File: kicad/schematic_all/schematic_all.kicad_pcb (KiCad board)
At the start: 2 copper layers, 88.9 x 88.9 mm, 31 parts, among them J1 Power In, SW1 Button 1, SW2 Encoder 1, SW3 Button 2, SW4 Encoder 2, SW5 Button 3, U2 RPi_Pico, U3 RDA5807M_Module, U4 LM386

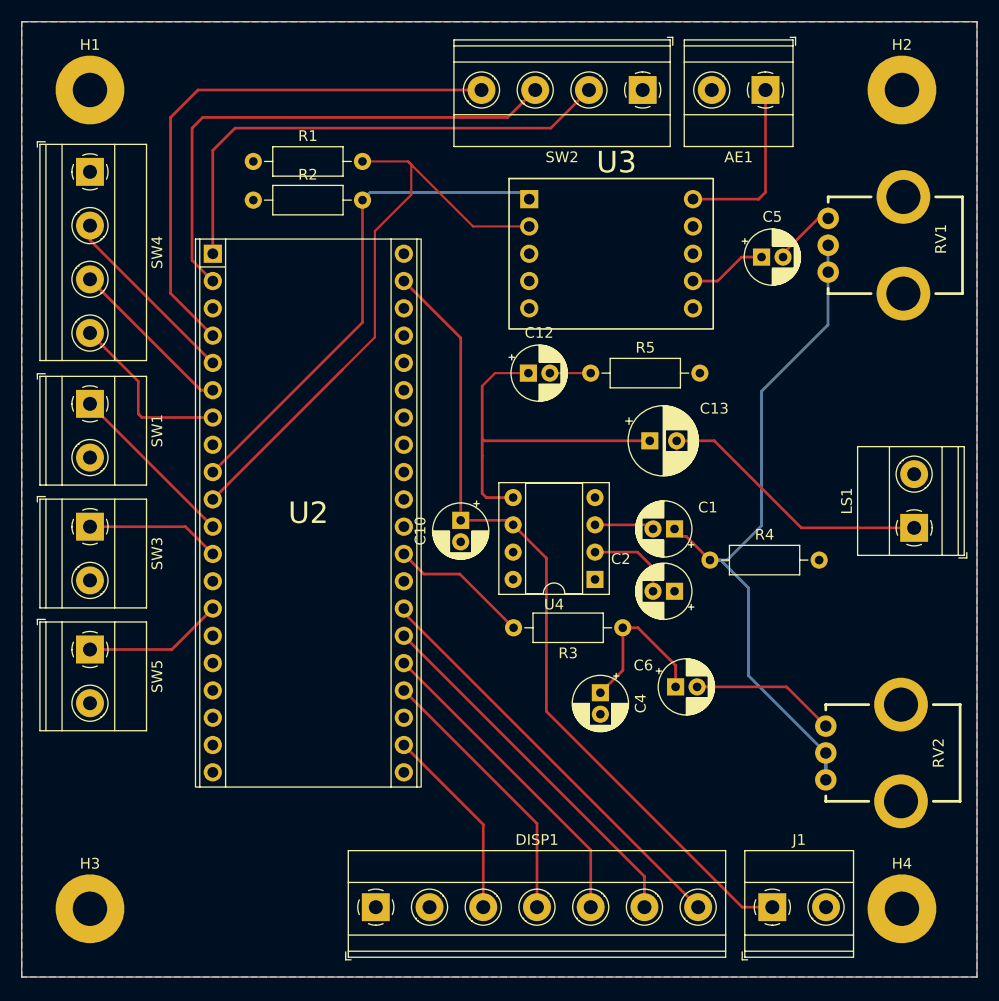
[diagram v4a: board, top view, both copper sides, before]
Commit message: Added 12V supply + linear regulator to step-down to 5V
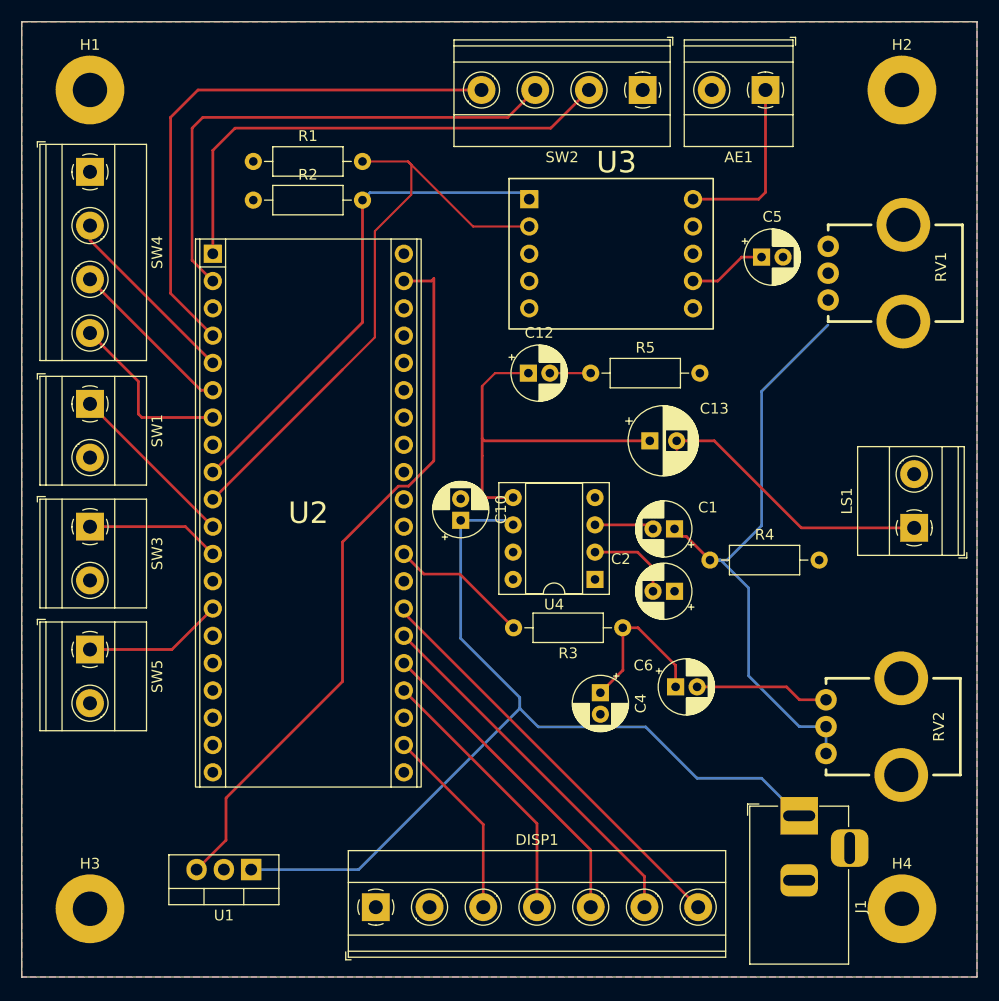
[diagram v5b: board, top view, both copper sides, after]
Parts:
- added U1: L7805, Package_TO_SOT_THT:TO-220-3_Vertical, F.Cu at (78.5, 117.0)
- J1: value Power In -> Barrel_Jack_MountingPin; footprint TerminalBlock_Phoenix:TerminalBlock_Phoenix_MKDS-1,5-2_1x02_P5.00mm_Horizontal -> Connector_BarrelJack:BarrelJack_Horizontal
- moved J1 8.86 mm to (129.5, 112.0), turned to 90 degrees
- moved RV1 2.60 mm to (132.2, 61.5)
- moved RV2 2.45 mm to (132.0, 103.7)
- turned C10 to 90 degrees
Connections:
- C10 pad 1: +5V -> +12V
- J1 pad 1: +5V -> +12V
- U4 pad 6: +5V -> +12V
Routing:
- net +12V: track 0.00 -> 86.8 mm
- net Net-(C1-Pad1): track 68.2 -> 56.4 mm
- net +5V: track 76.8 -> 67.6 mm
- net Net-(C5-Pad2): track 6.23 -> 0.32 mm
- net Net-(C6-Pad2): track 13.5 -> 12.5 mm

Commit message: Replaced jack with a terminal block
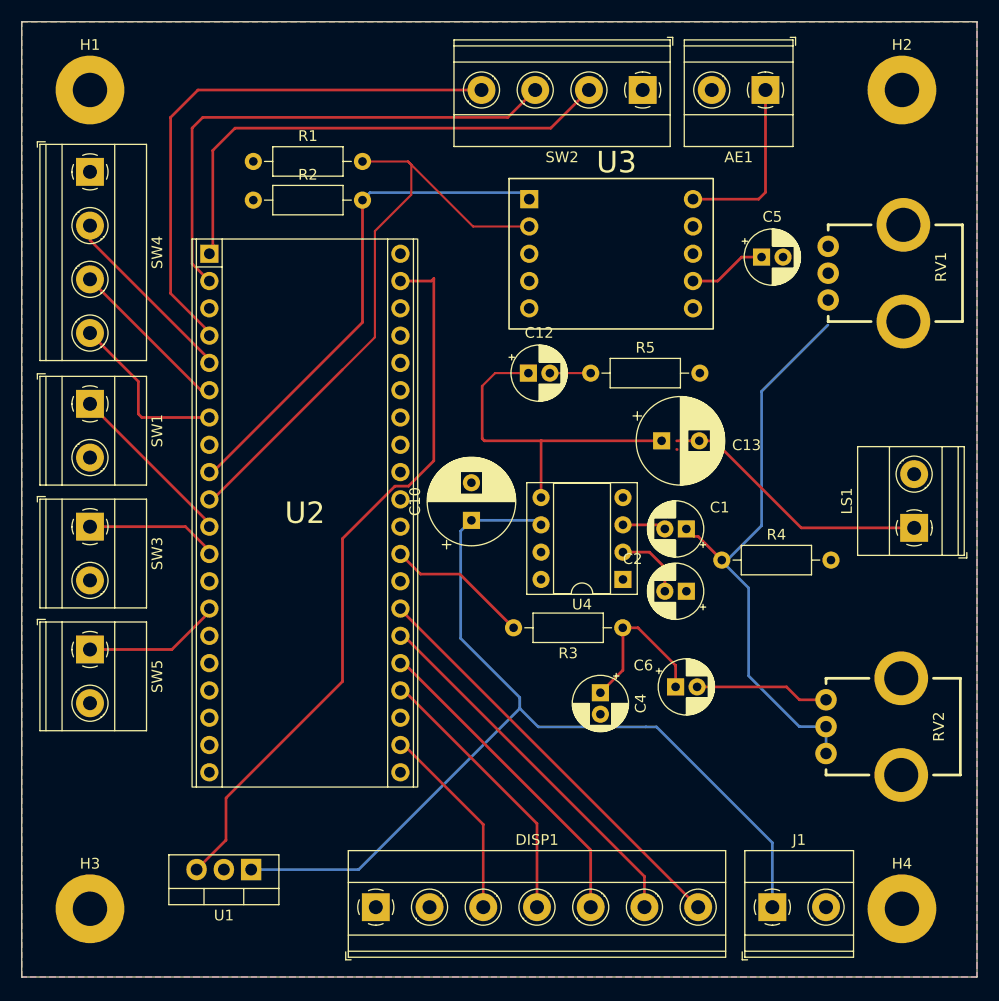
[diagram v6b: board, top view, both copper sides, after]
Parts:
- C10: value 10uF -> 680uF; footprint Capacitor_THT:CP_Radial_D5.0mm_P2.00mm -> Capacitor_THT:CP_Radial_D8.0mm_P3.50mm
- C13: footprint Capacitor_THT:CP_Radial_D6.3mm_P2.50mm -> Capacitor_THT:CP_Radial_D8.0mm_P3.50mm
- J1: value Barrel_Jack_MountingPin -> Screw_Terminal_01x02; footprint Connector_BarrelJack:BarrelJack_Horizontal -> TerminalBlock_Phoenix:TerminalBlock_Phoenix_MKDS-1,5-2_1x02_P5.00mm_Horizontal
- moved J1 8.86 mm to (127.0, 120.5), turned to 0 degrees
- moved U4 2.60 mm to (113.1, 90.0)
- moved C13 1.10 mm to (116.7, 77.1)
- moved C1 1.10 mm to (119.0, 85.3)
- moved C2 1.10 mm to (119.0, 91.1)
- moved R4 1.10 mm to (122.3, 88.2)
- moved C10 1.00 mm to (99.0, 84.5)
- moved U2 0.32 mm to (83.5, 83.8)
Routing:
- net +12V: track 86.8 -> 92.2 mm
- net Net-(C1-Pad1): track 56.4 -> 54.2 mm
- net Net-(C12-Pad1): track 34.2 -> 32.4 mm
- net Net-(U4--): track 8.20 -> 6.70 mm
- net Net-(U4-+): track 5.56 -> 4.06 mm
- net +5V: track 67.6 -> 68.1 mm

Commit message: fixes and cleanup of schematic
added in extra capacitors for linear regulator
cleaned up traces and aligned components
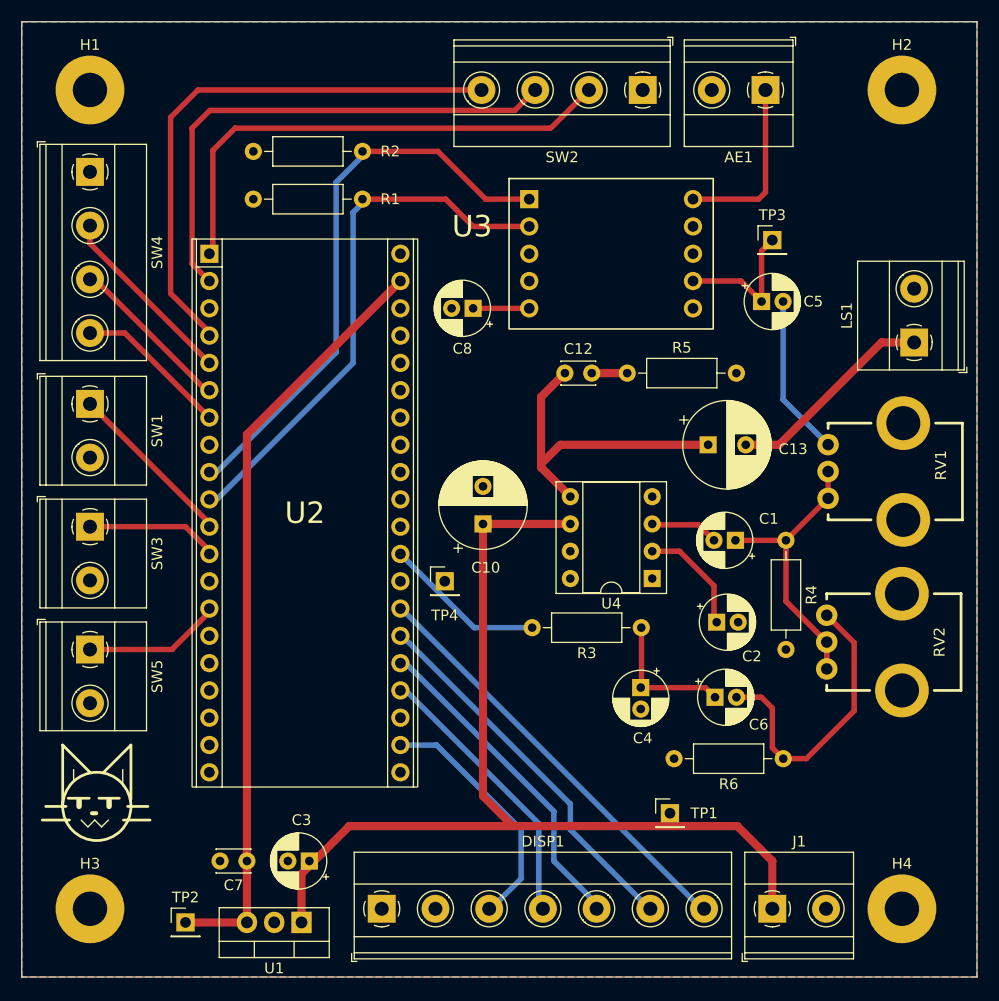
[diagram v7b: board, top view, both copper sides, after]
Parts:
- added C3: 220nF, Capacitor_THT:CP_Radial_D5.0mm_P2.00mm, F.Cu at (83.9, 116.2)
- added C7: 100nF, Capacitor_THT:C_Disc_D3.0mm_W2.0mm_P2.50mm, F.Cu at (78.1, 116.2)
- added C8: 100uF, Capacitor_THT:CP_Radial_D5.0mm_P2.00mm, F.Cu at (99.2, 64.8)
- added R6: 100k, Resistor_THT:R_Axial_DIN0207_L6.3mm_D2.5mm_P10.16mm_Horizontal, F.Cu at (128.0, 106.7)
- added TP1: TestPoint, Connector_PinHeader_2.54mm:PinHeader_1x01_P2.54mm_Vertical, F.Cu at (117.5, 111.8)
- added TP2: TestPoint, Connector_PinHeader_2.54mm:PinHeader_1x01_P2.54mm_Vertical, F.Cu at (72.4, 121.9)
- added TP3: TestPoint, Connector_PinHeader_2.54mm:PinHeader_1x01_P2.54mm_Vertical, F.Cu at (127.0, 58.4)
- added TP4: TestPoint, Connector_PinHeader_2.54mm:PinHeader_1x01_P2.54mm_Vertical, F.Cu at (96.5, 90.2)
- C12: footprint Capacitor_THT:CP_Radial_D5.0mm_P2.00mm -> Capacitor_THT:C_Disc_D3.0mm_W2.0mm_P2.50mm
- C4: value 100nF -> 1nF
- C6: value 100uF -> 1uF
- J1: value Screw_Terminal_01x02 -> Power In
- R3: value 220 -> 22k
- moved RV1 18.5 mm to (132.2, 80.0)
- moved LS1 17.3 mm to (140.2, 67.9)
- moved RV2 7.87 mm to (132.1, 95.8)
- moved U1 6.79 mm to (83.2, 121.9)
- moved R4 6.25 mm to (128.3, 86.4), turned to -90 degrees
- moved C1 4.69 mm to (123.6, 86.4)
- moved R2 4.54 mm to (78.7, 50.2)
- moved C13 4.35 mm to (121.0, 77.5)
- moved C5 4.14 mm to (126.0, 64.1)
- moved C2 4.03 mm to (121.8, 94.0), turned to 0 degrees
- moved C6 3.79 mm to (121.7, 101.0)
- moved C4 3.79 mm to (114.8, 100.1)
- moved R1 3.51 mm to (78.7, 54.6)
- moved C12 3.40 mm to (107.7, 70.8)
- moved R5 3.40 mm to (113.5, 70.8)
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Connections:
- C2 pad 1: GND -> Net-(U4--)
- C2 pad 2: Net-(U4--) -> GND
- RV1 pad 4: (no net) -> GND
- RV1 pad 5: (no net) -> GND
- RV2 pad 4: (no net) -> GND
- RV2 pad 5: (no net) -> GND
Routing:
- net Net-(C1-Pad1): track 54.2 -> 26.3 mm
- net Net-(C6-Pad2): track 12.5 -> 27.3 mm
- net Net-(C5-Pad2): track 0.32 -> 15.1 mm
- net /ISCL: track 57.4 -> 50.6 mm
- net /ISDA: track 47.5 -> 54.2 mm
- net /AOUT: track 7.30 -> 13.3 mm
- net Net-(C13-Pad2): track 25.5 -> 19.6 mm
- net +3.3V: track 0.00 -> 5.22 mm
- net /SCS: track 18.5 -> 22.7 mm
- net Net-(U4--): track 6.70 -> 10.5 mm
- net +5V: track 68.1 -> 71.3 mm
- net Net-(C12-Pad1): track 32.4 -> 29.8 mm
- net Net-(C4-Pad1): track 15.3 -> 12.9 mm
- net Net-(U4-+): track 4.06 -> 6.38 mm
- net /ENC2_PB: track 16.1 -> 14.4 mm
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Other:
- rule pad_to_mask_clearance: 0 -> 0.0508

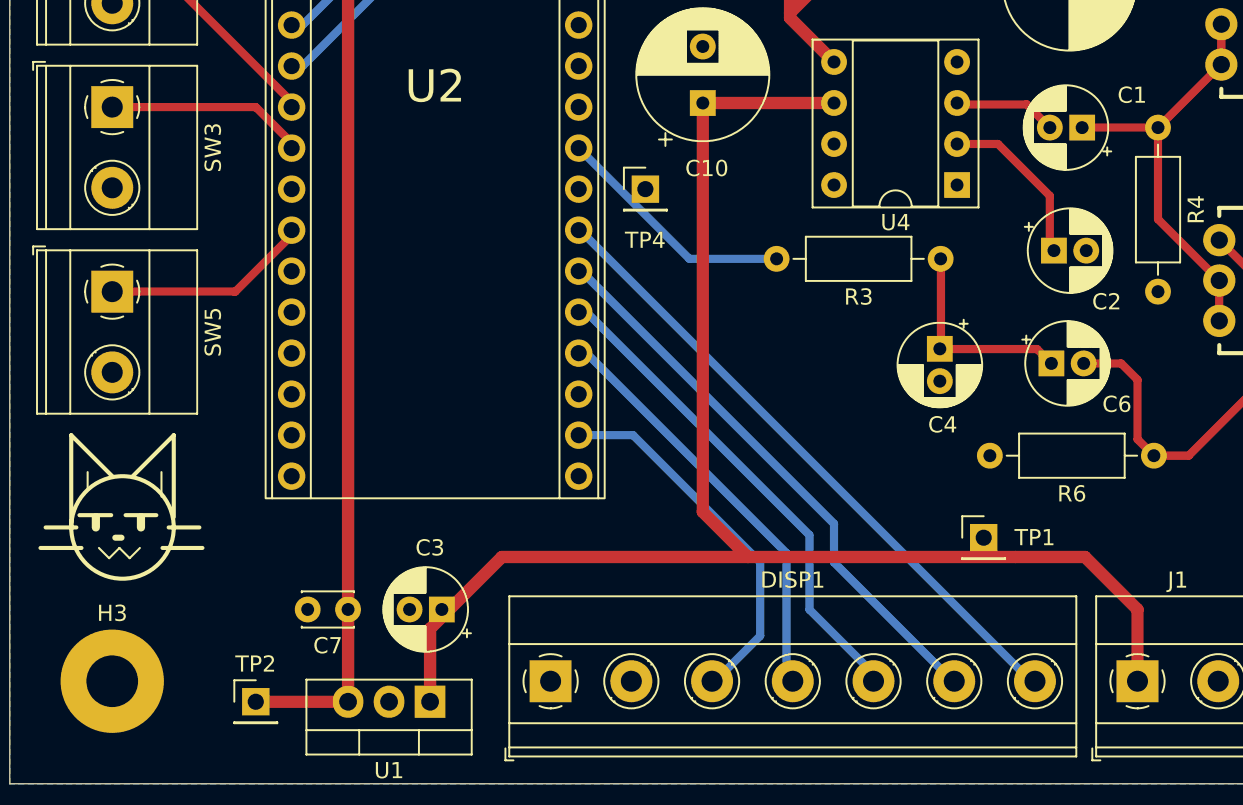
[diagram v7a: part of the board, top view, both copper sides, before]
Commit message: flip SPI and power traces
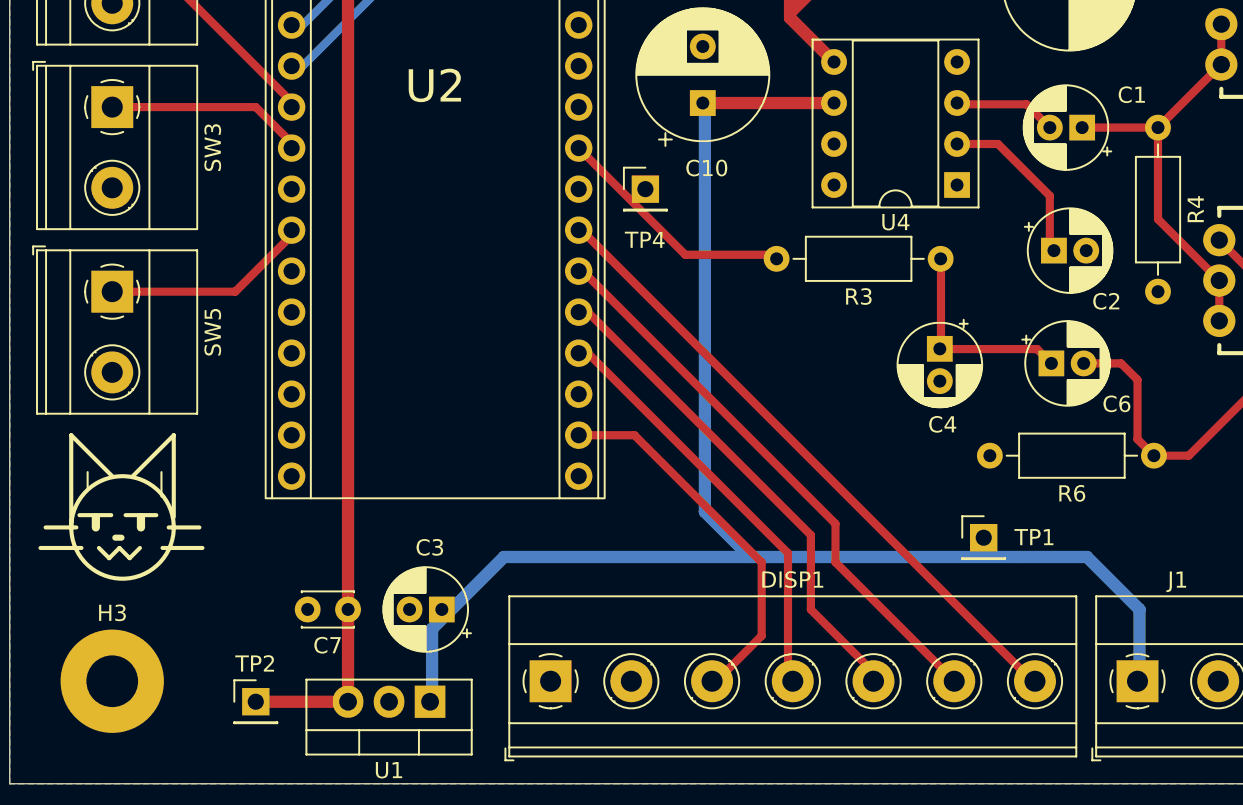
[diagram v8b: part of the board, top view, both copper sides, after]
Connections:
- RV1 pad 4: GND -> (no net)
- RV1 pad 5: GND -> (no net)
- RV2 pad 4: GND -> (no net)
- RV2 pad 5: GND -> (no net)
- U2 pad 35: GND -> unconnected-(U2-ADC_VREF-Pad35)
